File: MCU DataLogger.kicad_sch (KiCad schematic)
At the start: 25 parts, among them U1 24LC1025, U2 24LC1025, U3 DS1337S_, U4 ATMEGA328P-AU, Y1 32.768 KH, Y2 16MHz

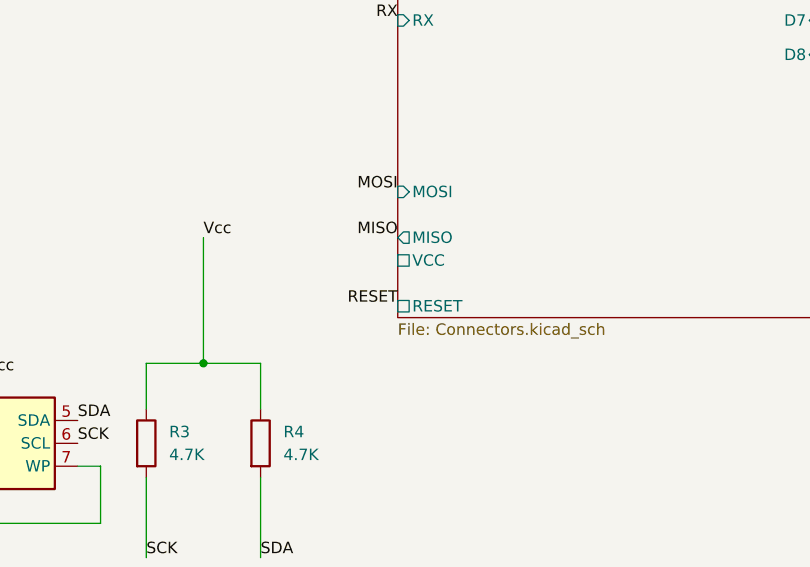
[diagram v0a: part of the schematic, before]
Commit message: Fixed the Erc pin not connected caused by capitalization error VCC vs Vcc
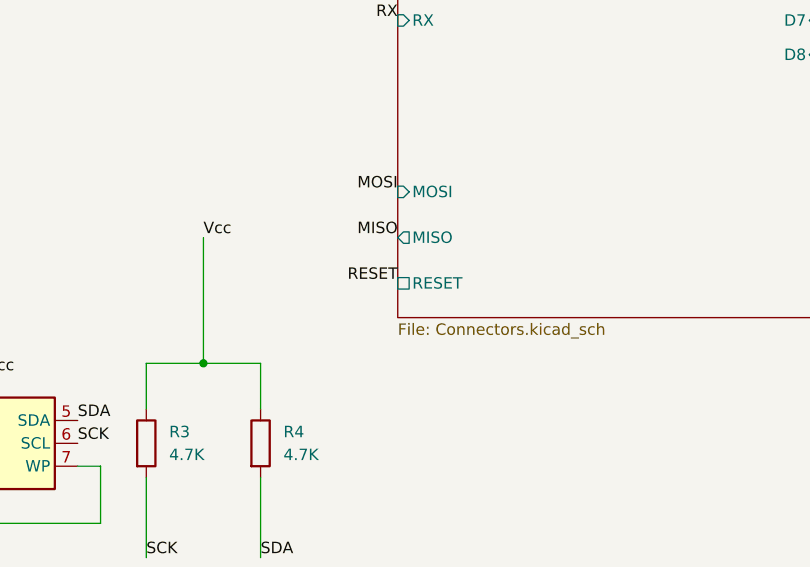
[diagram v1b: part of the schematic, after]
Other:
- sheet Connectors ports: added none; removed VCC
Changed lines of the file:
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@@
 	)
 	(label "RESET"
-		(at 127 149.86 180)
+		(at 127 147.32 180)
 		(effects
 			(font
@@
 		)
 		(pin "RESET" passive
-			(at 127 149.86 180)
+			(at 127 147.32 180)
 			(effects
 				(font
@@
 			(effects
 				(font
-					(size 1.27 1.27)
-				)
-				(justify left)
-			)
-		)
-		(pin "VCC" passive
-			(at 127 144.78 180)
-			(effects
-				(font

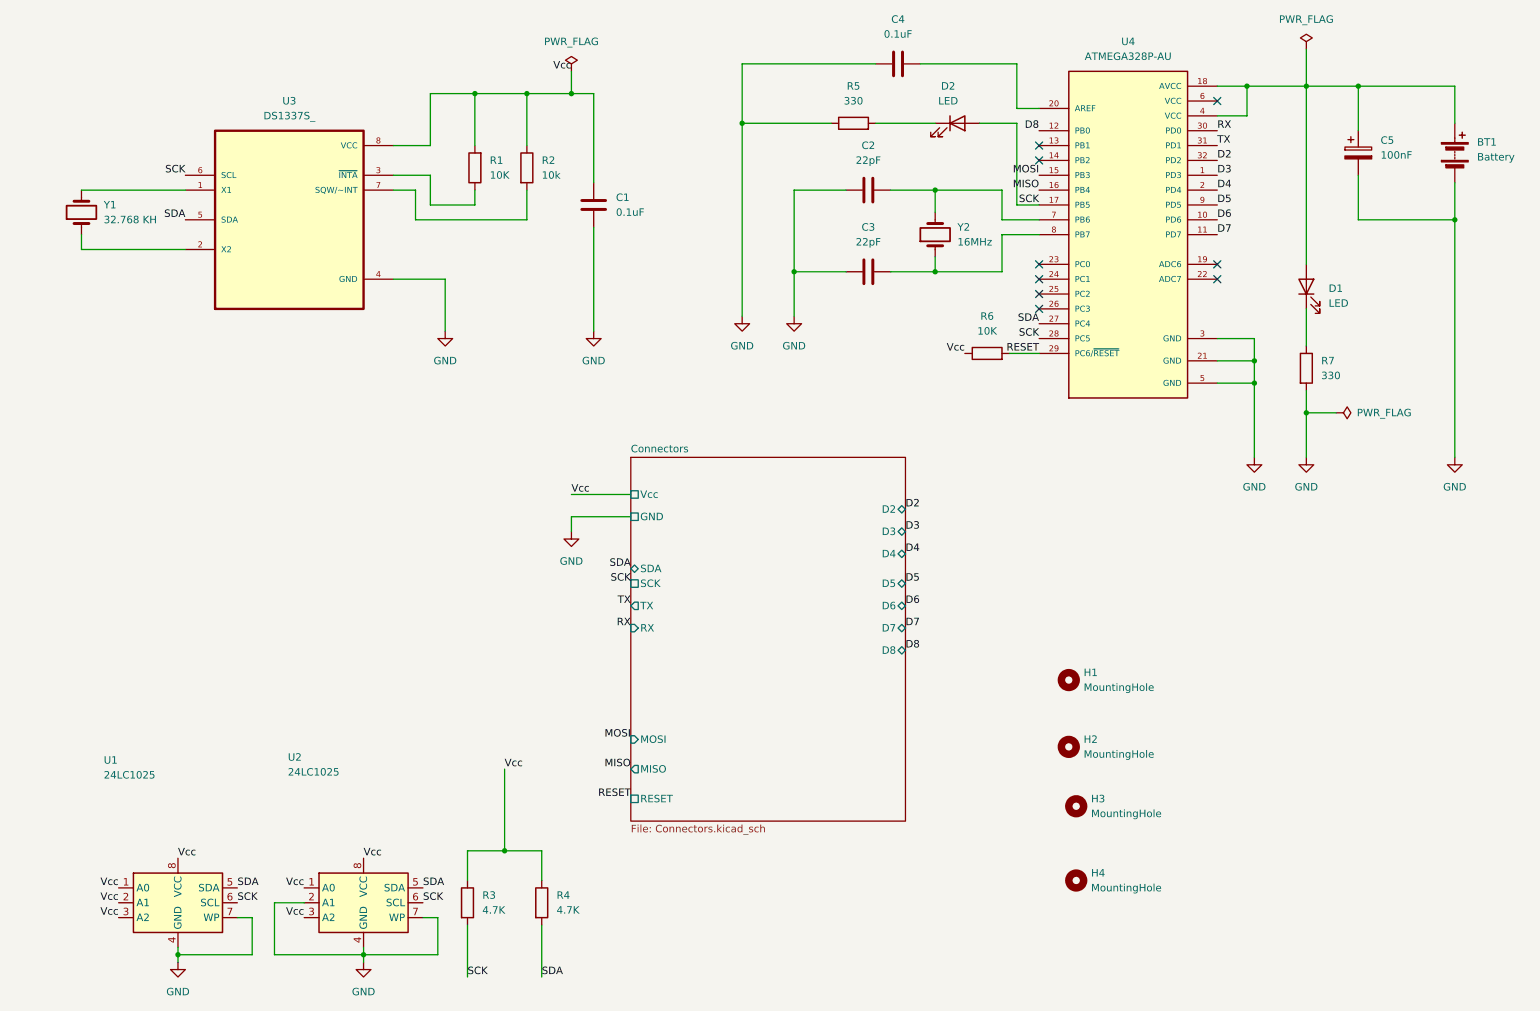
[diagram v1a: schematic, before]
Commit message: Completed the comments on the schematic sheet
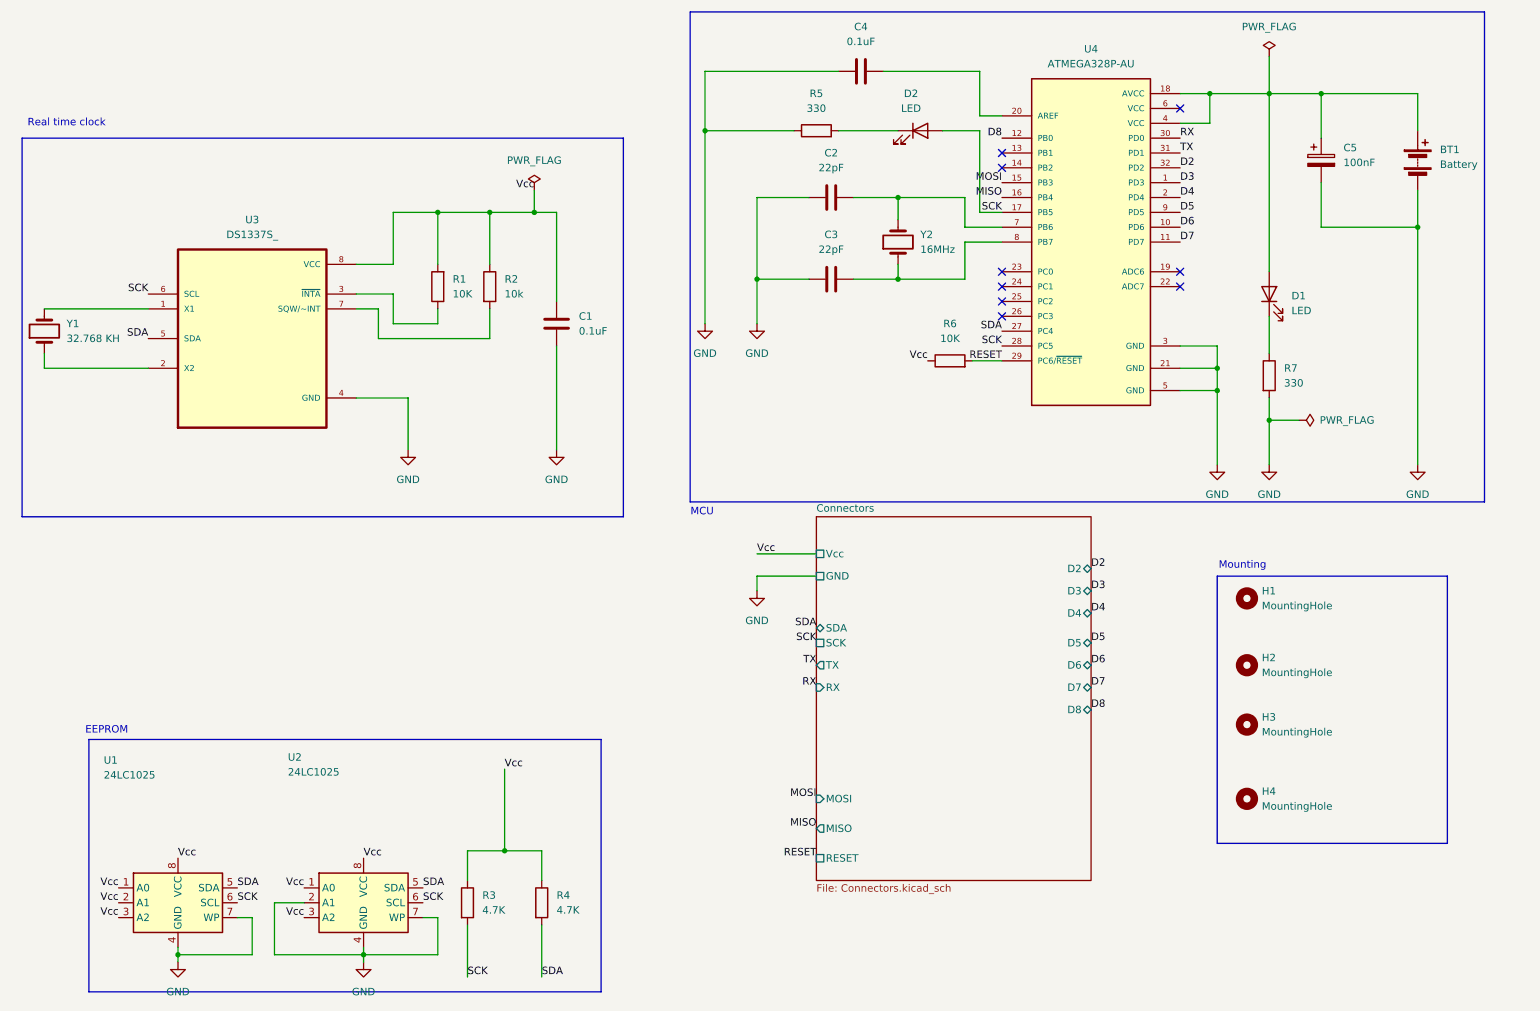
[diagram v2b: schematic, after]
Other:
- note added: "EEPROM"
- note added: "MCU"
- note added: "Mounting"
- note added: "Real time clock"
- moved on the sheet: BT1, C1, C2, C3, C4, C5, D1, D2, H1, H2, H3, H4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

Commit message: Added the footprint to U1 and U2, staging for pcb schematic import and layout
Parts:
- U1, U2: footprint (none) -> Package_SO:SOIC-8_5.3x5.3mm_P1.27mm
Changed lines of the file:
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@@
 			)
 		)
-		(property "Footprint" ""
+		(property "Footprint" "Package_SO:SOIC-8_5.3x5.3mm_P1.27mm"
 			(at 81.28 165.1 0)
 			(hide yes)
@@
 			)
 		)
-		(property "Footprint" ""
+		(property "Footprint" "Package_SO:SOIC-8_5.3x5.3mm_P1.27mm"
 			(at 49.53 165.1 0)
 			(hide yes)

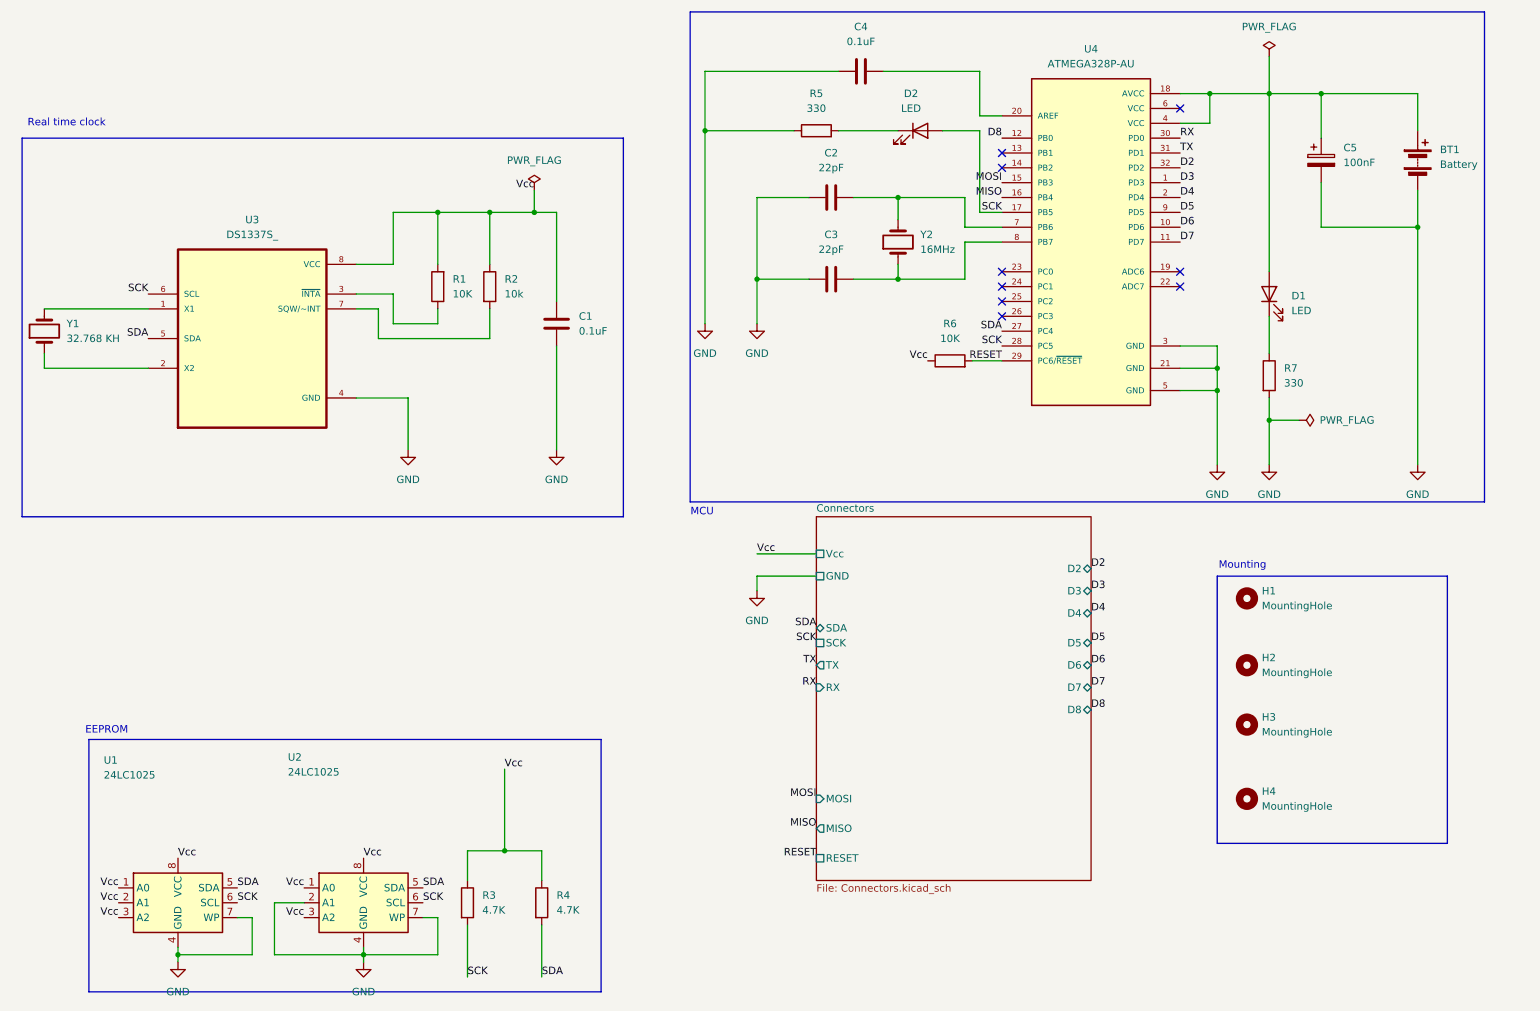
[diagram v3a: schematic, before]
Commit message: Resolved all the unconnected erc errors and assigned the propper cadd model for U2 and U4
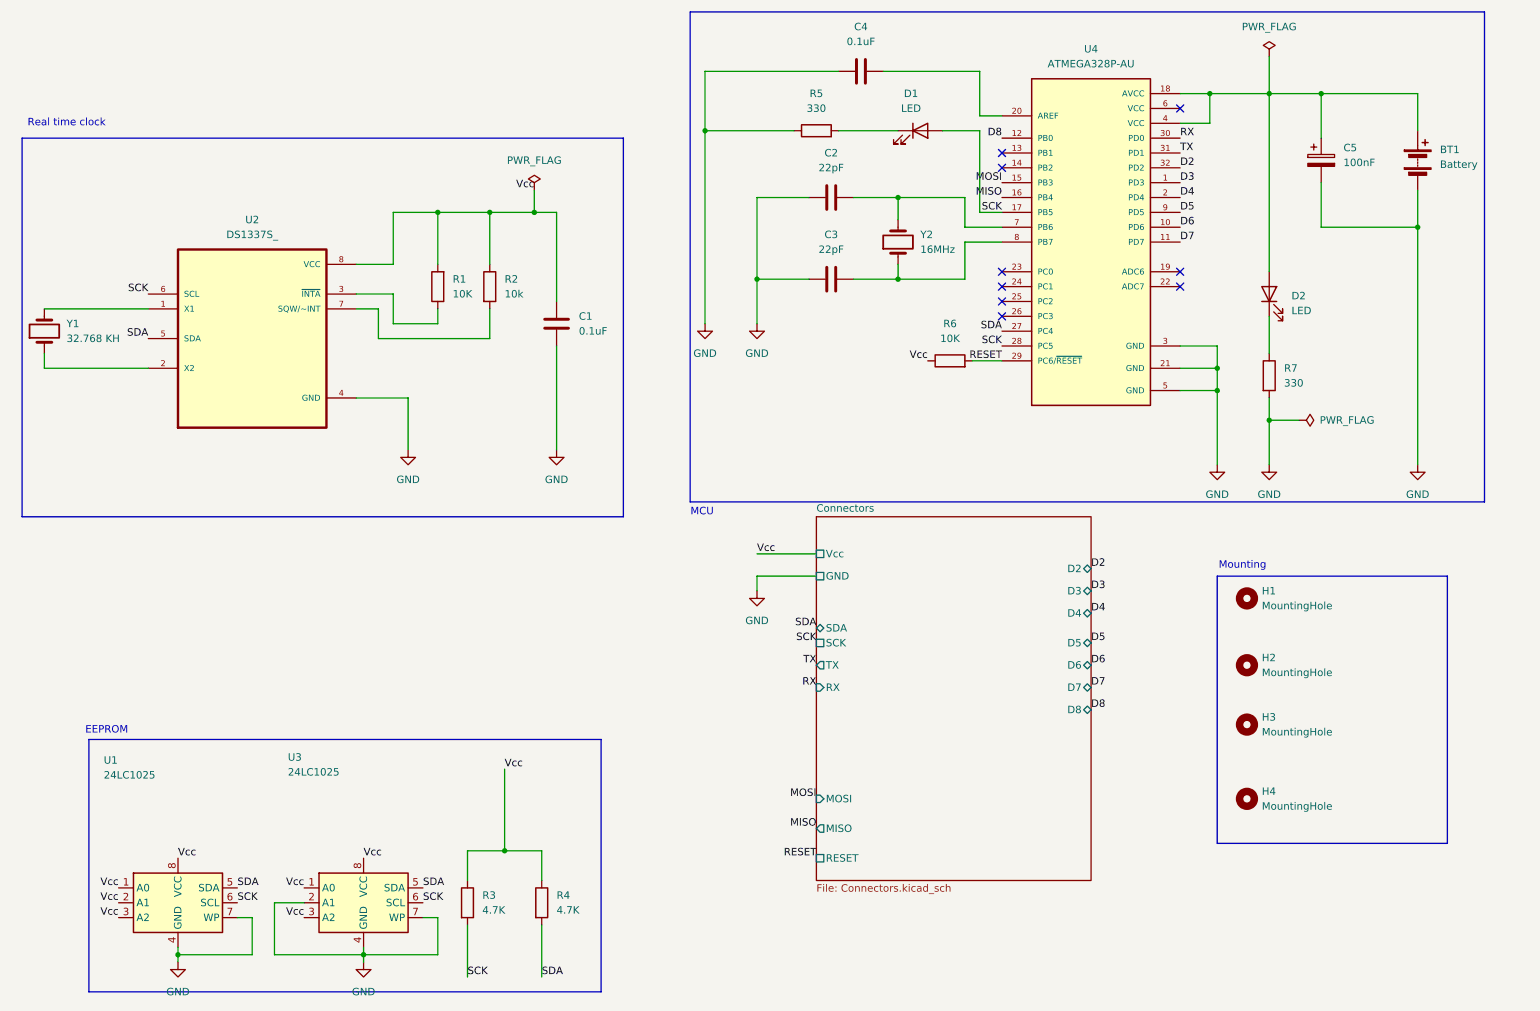
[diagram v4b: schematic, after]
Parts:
- renumbered D2 to D1, D1 to D2, U3 to U2, U2 to U3
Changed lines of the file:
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@@
 		(dnp no)
 		(fields_autoplaced yes)
-		(property "Reference" "D2"
+		(property "Reference" "D1"
 			(at 174.9425 26.67 0)
 			(show_name no)
@@
 			(project "MCU Datalogger"
 				(path "/82352dda-4ca1-40c9-b7a4-aaa22a39ffc1"
-					(reference "D2")
+					(reference "D1")
 					(unit 1)
 				)
@@
 		(dnp no)
 		(fields_autoplaced yes)
-		(property "Reference" "U3"
+		(property "Reference" "U2"
 			(at 62.23 48.26 0)
 			(show_name no)
@@
 			(project "MCU Datalogger"
 				(path "/82352dda-4ca1-40c9-b7a4-aaa22a39ffc1"
-					(reference "U3")
+					(reference "U2")
 					(unit 1)
 				)
@@
 		(in_pos_files yes)
 		(dnp no)
-		(property "Reference" "U2"
+		(property "Reference" "U3"
 			(at 68.326 140.208 0)
 			(show_name no)
@@
 			(project "MCU Datalogger"
 				(path "/82352dda-4ca1-40c9-b7a4-aaa22a39ffc1"
-					(reference "U2")
+					(reference "U3")
 					(unit 1)
 				)
@@
 		(dnp no)
 		(fields_autoplaced yes)
-		(property "Reference" "D1"
+		(property "Reference" "D2"
 			(at 240.03 61.2774 90)
 			(show_name no)
@@
 			(project "MCU Datalogger"
 				(path "/82352dda-4ca1-40c9-b7a4-aaa22a39ffc1"
-					(reference "D1")
+					(reference "D2")
 					(unit 1)
 				)
